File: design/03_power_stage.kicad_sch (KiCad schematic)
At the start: 55 parts, among them J301 PHASE_A, J302 PHASE_B, J303 PHASE_C, Q301 TPHR8504PL, Q302 TPHR8504PL, Q303 TPHR8504PL, Q304 TPHR8504PL, Q305 TPHR8504PL, Q306 TPHR8504PL, Q307 TPHR8504PL, Q308 TPHR8504PL, Q309 TPHR8504PL, Q310 TPHR8504PL, Q311 TPHR8504PL, Q312 TPHR8504PL

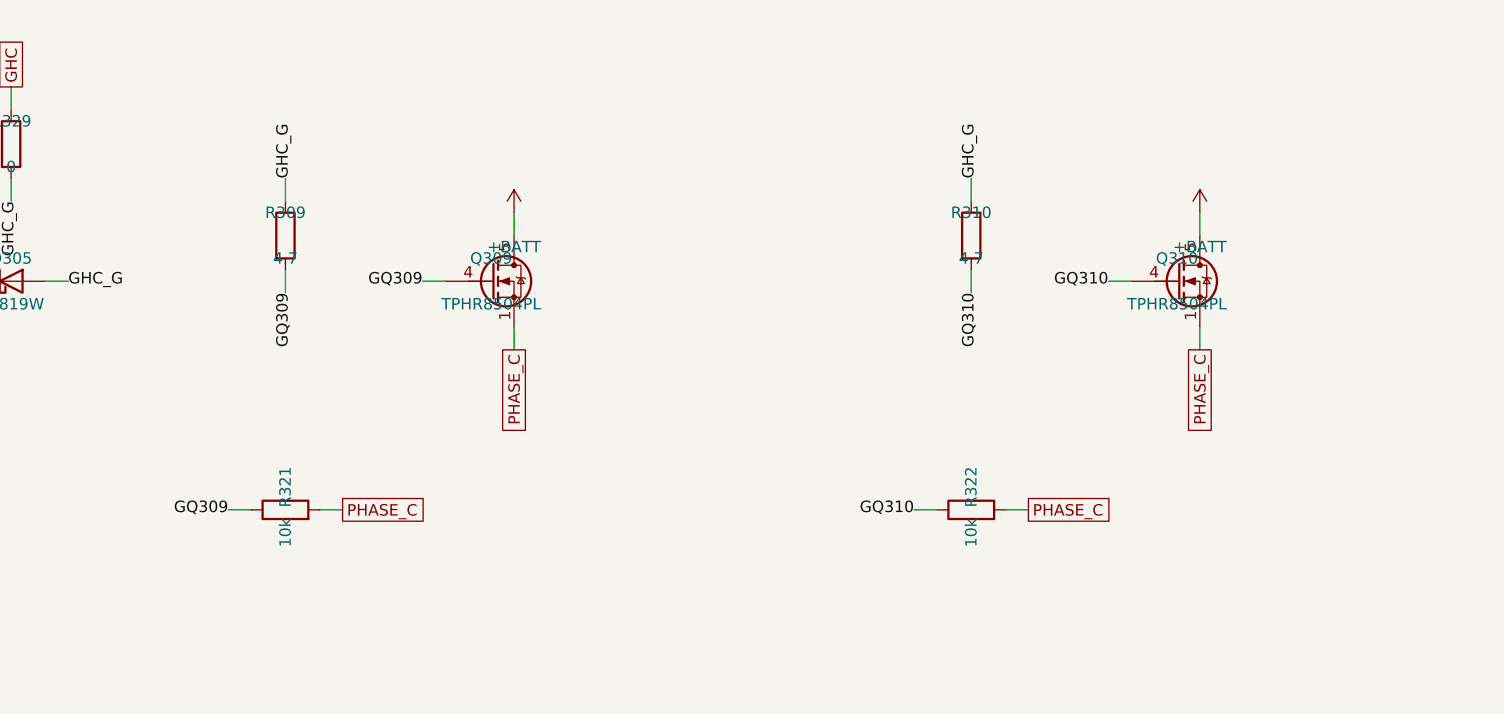
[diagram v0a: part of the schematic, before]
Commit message: PCB floorplan: 80x68 mm, 4-layer, all FETs on top over a tight ground plane
Places all 160 footprints, sets the stackup and board outline, and lands
DRC-clean at 0 violations (382 unconnected is expected -- nothing routed).

The layer split is the whole point, and it is not the one I first
suggested. Loop inductance is set by distance to the RETURN PLANE, not by
how the FETs are stacked:

    high side top / low side bottom   1.60 mm  4.36 nH  13.1 V overshoot
    all FETs top, return on B.Cu      1.60 mm  4.36 nH  13.1 V
    all FETs top, In1 at 0.5 mm       0.50 mm  1.36 nH   4.1 V
    all FETs top, In1 at 0.2 mm       0.20 mm  0.54 nH   1.6 V   <- this

Splitting the half-bridge across the board is intuitively appealing and
about 8x worse, because it forces the return through the full board
thickness. So all twelve FETs sit on F.Cu with an unbroken PGND plane
0.2 mm beneath them, and the stackup is asymmetric on purpose. At 150 A
with 50 ns edges (3 A/ns) that is 14.2 V peak on a 40 V FET instead of
25.7 V.

Floorplan: current flows straight down each phase column -- DC+ pour, 24
ceramics directly above the high-side drains, HS pair, phase pour, LS
pair, shunt, PGND. FETs are rotated 90 so the source/gate edge faces down
and the drain paddle faces the pour above it; rotating them the other way
doubles the loop area. Three B.Cu lanes carry each phase to its own motor
terminal, and all logic is consolidated at x < 29 to keep those lanes
clear.

Resolves ESC-004: the placeholder terminal was a 2.5 sqmm wire pad (~25 A)
with a 25 mm strain-relief tail, unplaceable and badly underrated.
Replaced with a generated 3.6 mm / 9 mm dual-sided land pattern for 8 AWG.

Resolves ESC-013 (new): KiCad's _ThermalVias variant of the DRV8323R
footprint embeds 0.2 mm vias, below the 0.3 mm realistic minimum for 2 oz
copper. Switched to the plain land pattern; thermal vias go in by hand.

Three pcbnew quirks worth knowing, all of which cost a debugging round:
board.Remove() invalidat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
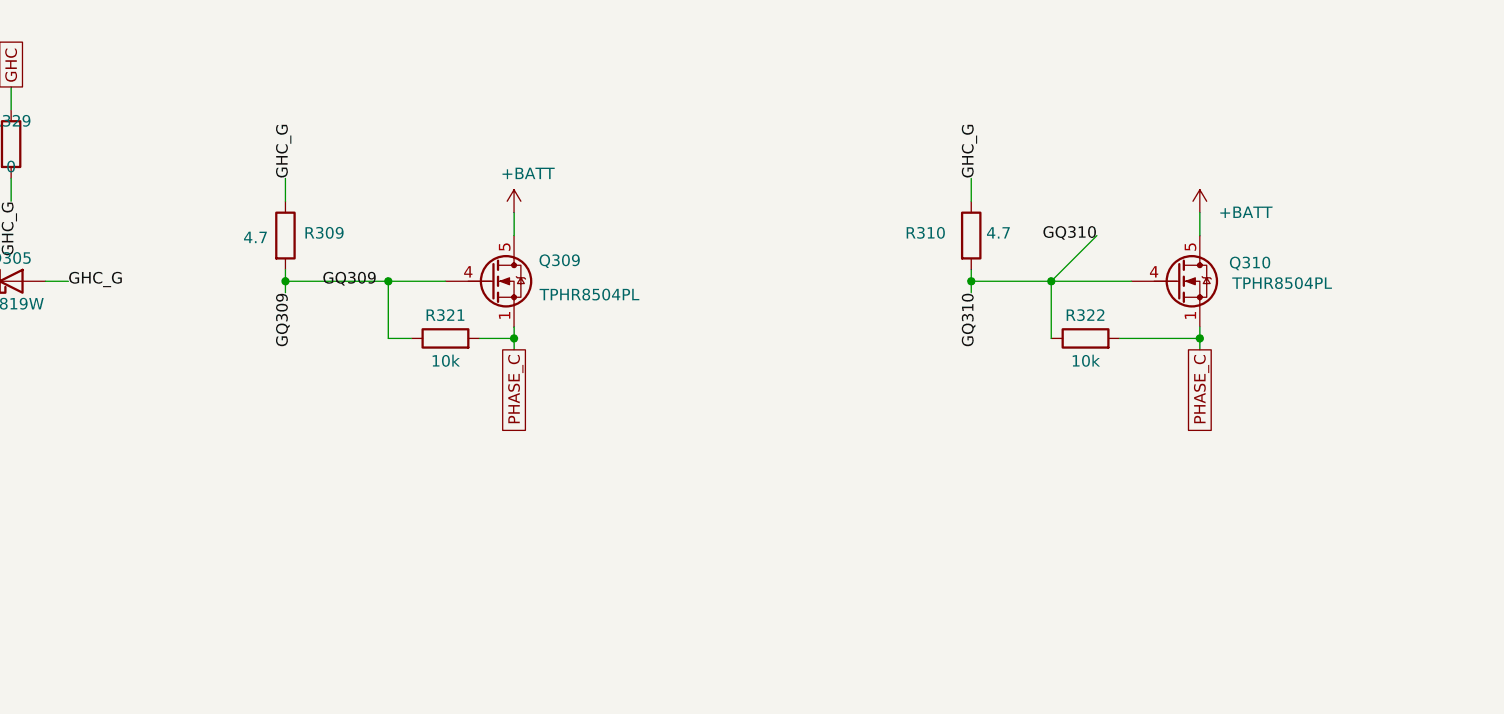
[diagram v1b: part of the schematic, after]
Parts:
- J301, J302, J303: footprint Connector_Wire:SolderWire-2.5sqmm_1x01_D2.4mm_OD3.6mm_Relief -> dshot-esc-100a:HighCurrentTerminal_8AWG
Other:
- moved on the sheet: R322
